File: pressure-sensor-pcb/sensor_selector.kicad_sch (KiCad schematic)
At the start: 14 parts

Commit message: add footprints
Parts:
- R? (x4): footprint (none) -> Resistor_THT:R_Axial_DIN0204_L3.6mm_D1.6mm_P7.62mm_Horizontal
- U? (x2): footprint (none) -> Package_SO:SO-14_3.9x8.65mm_P1.27mm
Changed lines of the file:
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@@
       (effects (font (size 1.27 1.27)) (justify left))
     )
-    (property "Footprint" "" (id 2) (at 128.27 128.27 0)
+    (property "Footprint" "Package_SO:SO-14_3.9x8.65mm_P1.27mm" (id 2) (at 128.27 128.27 0)
       (effects (font (size 1.27 1.27)) hide)
     )
@@
     (property "Reference" "R?" (id 0) (at 99.06 66.04 90))
     (property "Value" "1M" (id 1) (at 99.06 68.58 90))
-    (property "Footprint" "" (id 2) (at 99.06 74.168 90)
+    (property "Footprint" "Resistor_THT:R_Axial_DIN0204_L3.6mm_D1.6mm_P7.62mm_Horizontal" (id 2) (at 99.06 74.168 90)
       (effects (font (size 1.27 1.27)) hide)
     )
@@
     (property "Reference" "R?" (id 0) (at 99.06 87.63 90))
     (property "Value" "100K" (id 1) (at 99.06 90.17 90))
-    (property "Footprint" "" (id 2) (at 99.06 95.758 90)
+    (property "Footprint" "Resistor_THT:R_Axial_DIN0204_L3.6mm_D1.6mm_P7.62mm_Horizontal" (id 2) (at 99.06 95.758 90)
       (effects (font (size 1.27 1.27)) hide)
     )
@@
     (property "Reference" "R?" (id 0) (at 99.06 109.22 90))
     (property "Value" "10K" (id 1) (at 99.06 111.76 90))
-    (property "Footprint" "" (id 2) (at 99.06 117.348 90)
+    (property "Footprint" "Resistor_THT:R_Axial_DIN0204_L3.6mm_D1.6mm_P7.62mm_Horizontal" (id 2) (at 99.06 117.348 90)
       (effects (font (size 1.27 1.27)) hide)
     )
@@
     (property "Reference" "R?" (id 0) (at 99.06 43.18 90))
     (property "Value" "10M" (id 1) (at 99.06 45.72 90))
-    (property "Footprint" "" (id 2) (at 99.06 51.308 90)
+    (property "Footprint" "Resistor_THT:R_Axial_DIN0204_L3.6mm_D1.6mm_P7.62mm_Horizontal" (id 2) (at 99.06 51.308 90)
       (effects (font (size 1.27 1.27)) hide)
     )
@@
       (effects (font (size 1.27 1.27)) (justify left))
     )
-    (property "Footprint" "" (id 2) (at 95.25 128.27 0)
-      (effects (font (size 1.27 1.27)) hide)
-    )
+    (property "Footprint" "Package_SO:SO-14_3.9x8.65mm_P1.27mm" (id 2) (at 95.25 128.27 0)
+      (effects (font (size 1.27 1.27)) hide)
+    )

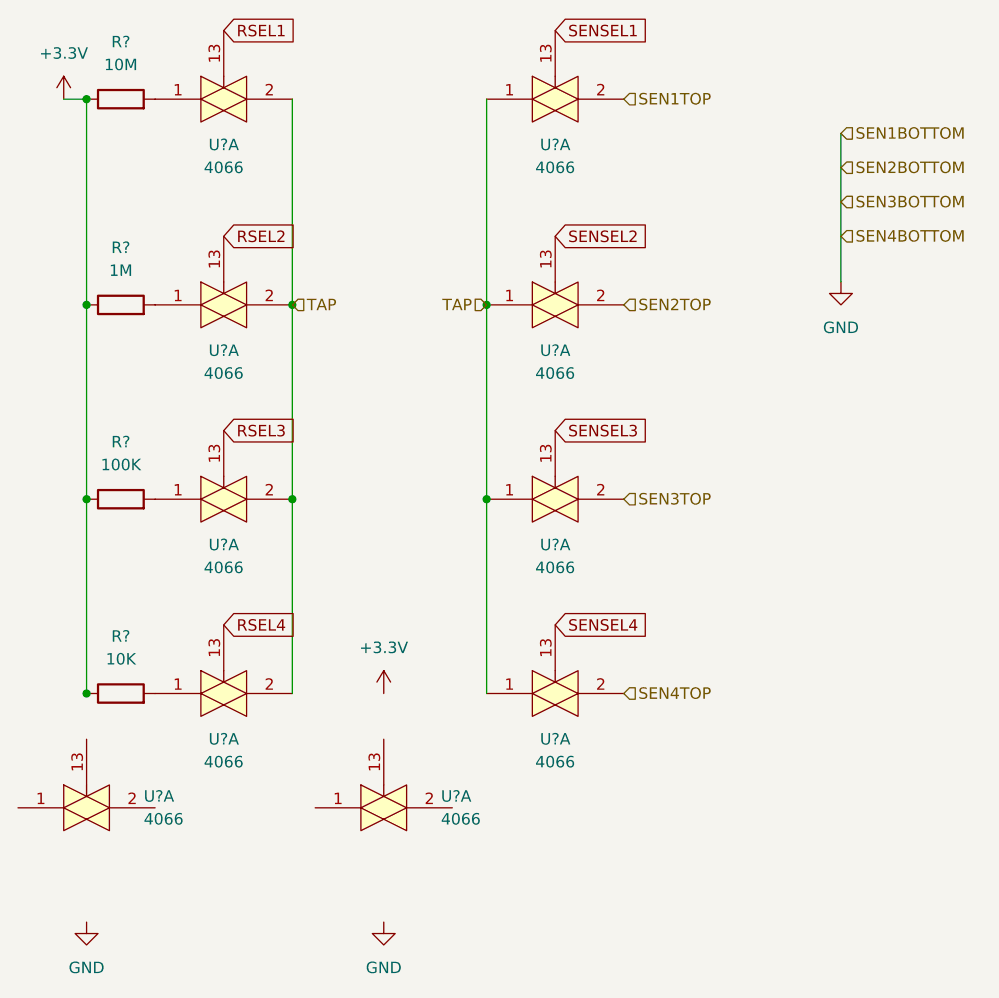
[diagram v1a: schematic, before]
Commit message: test initial PCB layout for fit
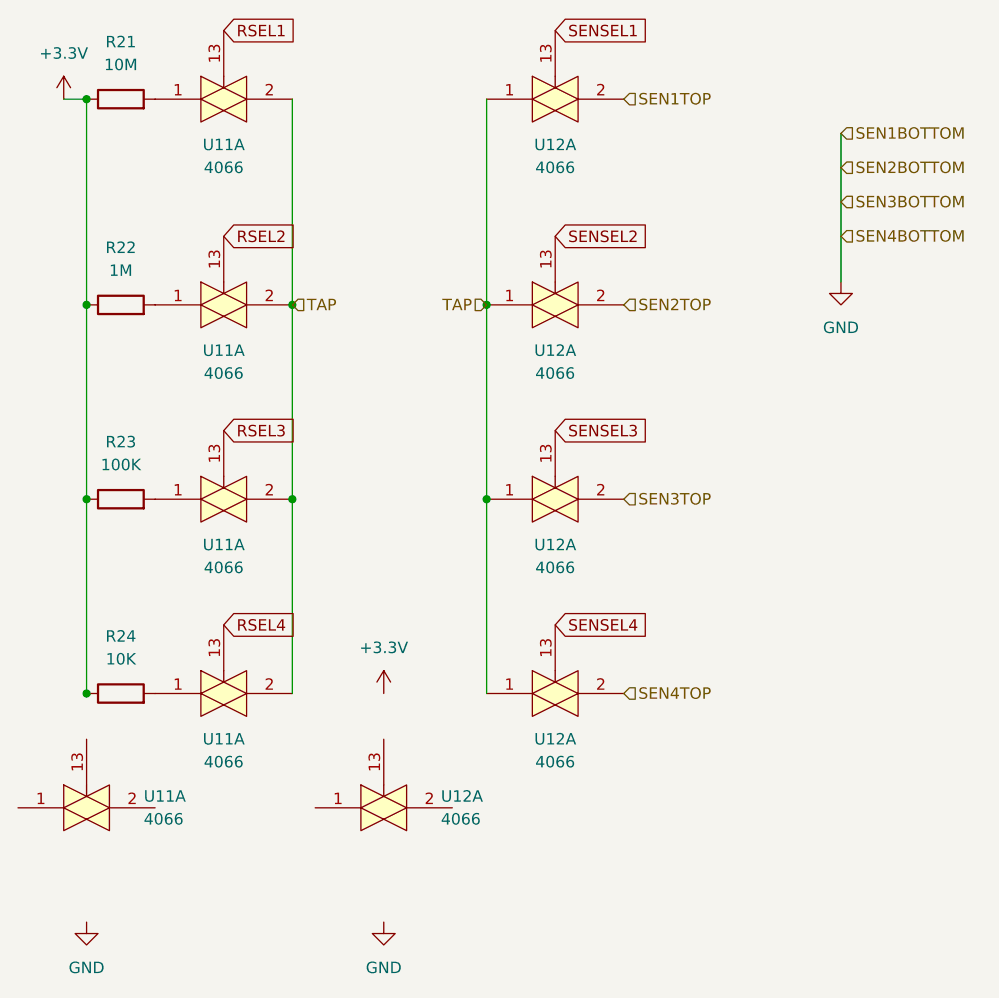
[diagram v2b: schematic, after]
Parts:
- gave numbers to parts that had none: 6
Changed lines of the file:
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@@
   (symbol (lib_id "4xxx:4066") (at 128.27 128.27 0)
     (in_bom yes) (on_board yes) (fields_autoplaced)
-    (property "Reference" "U?" (id 0) (at 134.62 126.9999 0)
+    (property "Reference" "U12" (id 0) (at 134.62 126.9999 0)
       (effects (font (size 1.27 1.27)) (justify left))
     )
@@
   (symbol (lib_id "4xxx:4066") (at 110.49 93.98 0)
     (in_bom yes) (on_board yes) (fields_autoplaced)
-    (property "Reference" "U?" (id 0) (at 110.49 99.06 0))
+    (property "Reference" "U11" (id 0) (at 110.49 99.06 0))
     (property "Value" "4066" (id 1) (at 110.49 101.6 0))
     (property "Footprint" "" (id 2) (at 110.49 93.98 0)
@@
   (symbol (lib_id "power:+3.3V") (at 92.71 49.53 0)
     (in_bom yes) (on_board yes) (fields_autoplaced)
-    (property "Reference" "#PWR?" (id 0) (at 92.71 53.34 0)
+    (property "Reference" "#PWR028" (id 0) (at 92.71 53.34 0)
       (effects (font (size 1.27 1.27)) hide)
     )
@@
   (symbol (lib_id "4xxx:4066") (at 110.49 49.53 0)
     (in_bom yes) (on_board yes) (fields_autoplaced)
-    (property "Reference" "U?" (id 0) (at 110.49 54.61 0))
+    (property "Reference" "U11" (id 0) (at 110.49 54.61 0))
     (property "Value" "4066" (id 1) (at 110.49 57.15 0))
     (property "Footprint" "" (id 2) (at 110.49 49.53 0)
@@
   (symbol (lib_id "4xxx:4066") (at 110.49 72.39 0)
     (in_bom yes) (on_board yes) (fields_autoplaced)
-    (property "Reference" "U?" (id 0) (at 110.49 77.47 0))
+    (property "Reference" "U11" (id 0) (at 110.49 77.47 0))
     (property "Value" "4066" (id 1) (at 110.49 80.01 0))
     (property "Footprint" "" (id 2) (at 110.49 72.39 0)
@@
   (symbol (lib_id "power:GND") (at 179.07 69.85 0)
     (in_bom yes) (on_board yes) (fields_autoplaced)
-    (property "Reference" "#PWR?" (id 0) (at 179.07 76.2 0)
+    (property "Reference" "#PWR032" (id 0) (at 179.07 76.2 0)
       (effects (font (size 1.27 1.27)) hide)
     )
@@
   (symbol (lib_id "Device:R") (at 99.06 72.39 90)
     (in_bom yes) (on_board yes) (fields_autoplaced)
-    (property "Reference" "R?" (id 0) (at 99.06 66.04 90))
+    (property "Reference" "R22" (id 0) (at 99.06 66.04 90))
     (property "Value" "1M" (id 1) (at 99.06 68.58 90))
     (property "Footprint" "Resistor_THT:R_Axial_DIN0204_L3.6mm_D1.6mm_P7.62mm_Horizontal" (id 2) (at 99.06 74.168 90)
@@
   (symbol (lib_id "power:GND") (at 128.27 140.97 0)
     (in_bom yes) (on_board yes) (fields_autoplaced)
-    (property "Reference" "#PWR?" (id 0) (at 128.27 147.32 0)
+    (property "Reference" "#PWR031" (id 0) (at 128.27 147.32 0)
       (effects (font (size 1.27 1.27)) hide)
     )
@@
   (symbol (lib_id "Device:R") (at 99.06 93.98 90)
     (in_bom yes) (on_board yes) (fields_autoplaced)
-    (property "Reference" "R?" (id 0) (at 99.06 87.63 90))
+    (property "Reference" "R23" (id 0) (at 99.06 87.63 90))
     (property "Value" "100K" (id 1) (at 99.06 90.17 90))
     (property "Footprint" "Resistor_THT:R_Axial_DIN0204_L3.6mm_D1.6mm_P7.62mm_Horizontal" (id 2) (at 99.06 95.758 90)
@@
   (symbol (lib_id "4xxx:4066") (at 147.32 49.53 0)
     (in_bom yes) (on_board yes) (fields_autoplaced)
-    (property "Reference" "U?" (id 0) (at 147.32 54.61 0))
+    (property "Reference" "U12" (id 0) (at 147.32 54.61 0))
     (property "Value" "4066" (id 1) (at 147.32 57.15 0))
     (property "Footprint" "" (id 2) (at 147.32 49.53 0)
@@
   (symbol (lib_id "Device:R") (at 99.06 115.57 90)
     (in_bom yes) (on_board yes) (fields_autoplaced)
-    (property "Reference" "R?" (id 0) (at 99.06 109.22 90))
+    (property "Reference" "R24" (id 0) (at 99.06 109.22 90))
     (property "Value" "10K" (id 1) (at 99.06 111.76 90))
     (property "Footprint" "Resistor_THT:R_Axial_DIN0204_L3.6mm_D1.6mm_P7.62mm_Horizontal" (id 2) (at 99.06 117.348 90)
@@
   (symbol (lib_id "4xxx:4066") (at 110.49 115.57 0)
     (in_bom yes) (on_board yes) (fields_autoplaced)
-    (property "Reference" "U?" (id 0) (at 110.49 120.65 0))
+    (property "Reference" "U11" (id 0) (at 110.49 120.65 0))
     (property "Value" "4066" (id 1) (at 110.49 123.19 0))
     (property "Footprint" "" (id 2) (at 110.49 115.57 0)
@@
   (symbol (lib_id "Device:R") (at 99.06 49.53 90)
     (in_bom yes) (on_board yes) (fields_autoplaced)
-    (property "Reference" "R?" (id 0) (at 99.06 43.18 90))
+    (property "Reference" "R21" (id 0) (at 99.06 43.18 90))
     (property "Value" "10M" (id 1) (at 99.06 45.72 90))
     (property "Footprint" "Resistor_THT:R_Axial_DIN0204_L3.6mm_D1.6mm_P7.62mm_Horizontal" (id 2) (at 99.06 51.308 90)
@@
   (symbol (lib_id "power:GND") (at 95.25 140.97 0)
     (in_bom yes) (on_board yes) (fields_autoplaced)
-    (property "Reference" "#PWR?" (id 0) (at 95.25 147.32 0)
+    (property "Reference" "#PWR029" (id 0) (at 95.25 147.32 0)
       (effects (font (size 1.27 1.27)) hide)
     )
@@
   (symbol (lib_id "power:+3.3V") (at 128.27 115.57 0)
     (in_bom yes) (on_board yes) (fields_autoplaced)
-    (property "Reference" "#PWR?" (id 0) (at 128.27 119.38 0)
+    (property "Reference" "#PWR030" (id 0) (at 128.27 119.38 0)
       (effects (font (size 1.27 1.27)) hide)
     )
@@
   (symbol (lib_id "4xxx:4066") (at 147.32 72.39 0)
     (in_bom yes) (on_board yes) (fields_autoplaced)
-    (property "Reference" "U?" (id 0) (at 147.32 77.47 0))
+    (property "Reference" "U12" (id 0) (at 147.32 77.47 0))
     (property "Value" "4066" (id 1) (at 147.32 80.01 0))
     (property "Footprint" "" (id 2) (at 147.32 72.39 0)
@@
   (symbol (lib_id "4xxx:4066") (at 147.32 115.57 0)
     (in_bom yes) (on_board yes) (fields_autoplaced)
-    (property "Reference" "U?" (id 0) (at 147.32 120.65 0))
+    (property "Reference" "U12" (id 0) (at 147.32 120.65 0))
     (property "Value" "4066" (id 1) (at 147.32 123.19 0))
     (property "Footprint" "" (id 2) (at 147.32 115.57 0)
@@
   (symbol (lib_id "4xxx:4066") (at 147.32 93.98 0)
     (in_bom yes) (on_board yes) (fields_autoplaced)
-    (property "Reference" "U?" (id 0) (at 147.32 99.06 0))
+    (property "Reference" "U12" (id 0) (at 147.32 99.06 0))
     (property "Value" "4066" (id 1) (at 147.32 101.6 0))
     (property "Footprint" "" (id 2) (at 147.32 93.98 0)
@@
   (symbol (lib_id "4xxx:4066") (at 95.25 128.27 0)
     (in_bom yes) (on_board yes) (fields_autoplaced)
-    (property "Reference" "U?" (id 0) (at 101.6 126.9999 0)
+    (property "Reference" "U11" (id 0) (at 101.6 126.9999 0)
       (effects (font (size 1.27 1.27)) (justify left))
     )
